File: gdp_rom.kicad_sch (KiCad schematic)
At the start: 19 parts, among them J10 Conn_01x02_Male, J3 Conn_02x25_Counter_Clockwise, J4 Conn_02x25_Counter_Clockwise, U14 74LS05, U18 74LS374, U29 2332A, U39 74LS138, U40 74LS20, U5 74LS08, U6 74LS32, U9 EF936x

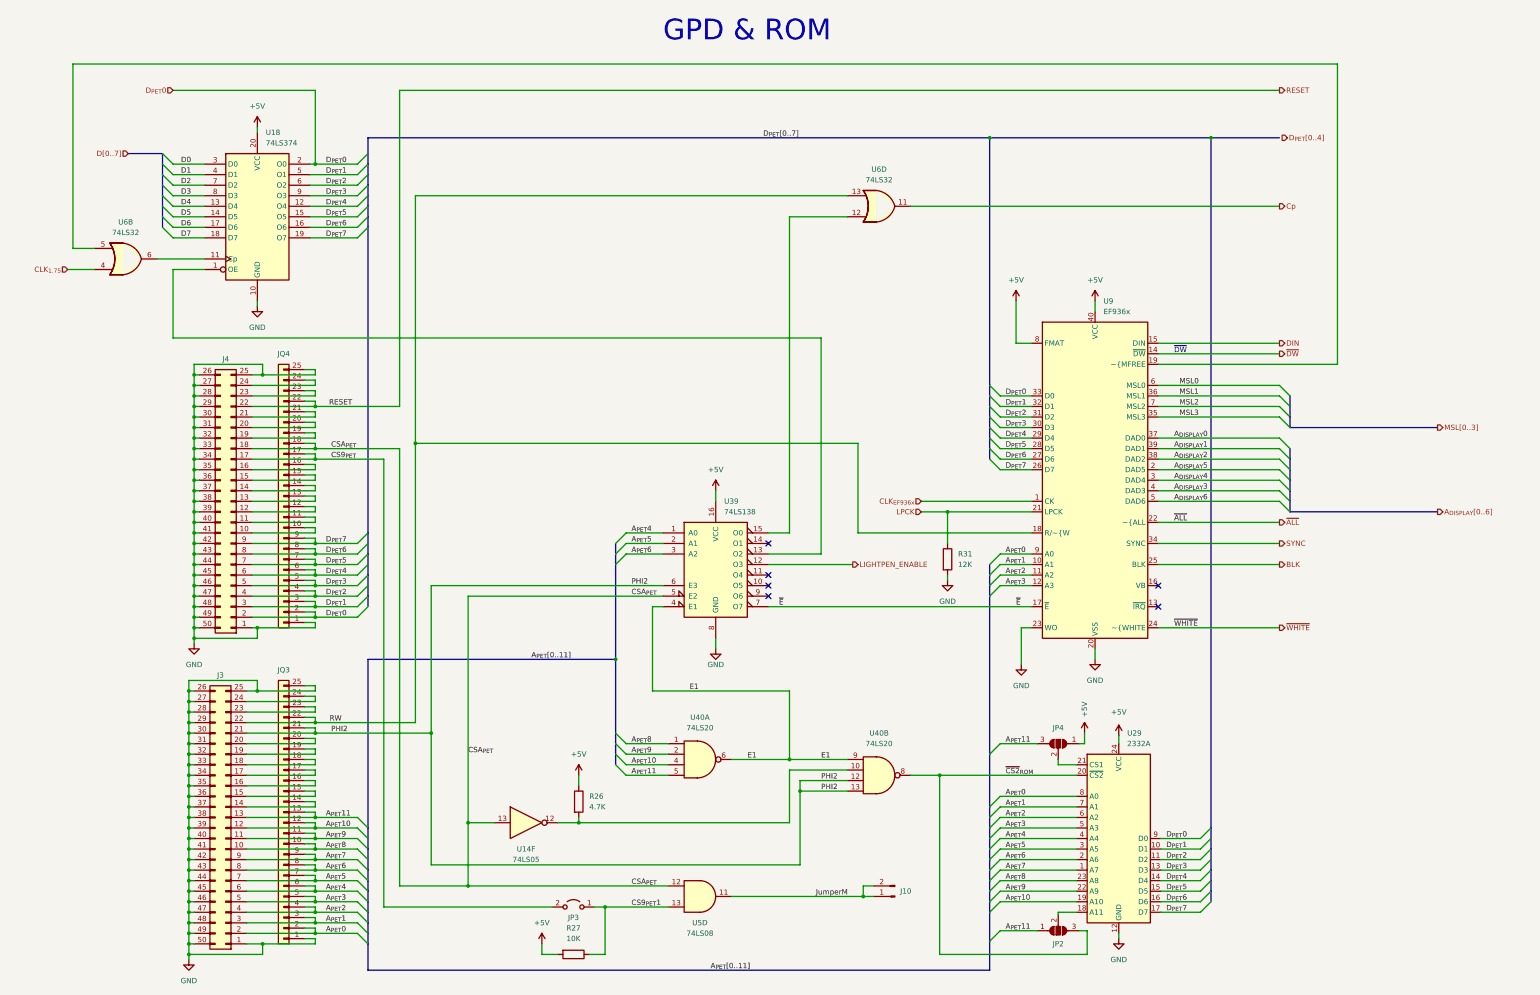
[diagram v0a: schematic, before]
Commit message: Improved signal naming
clearer naming of some signals for better readability
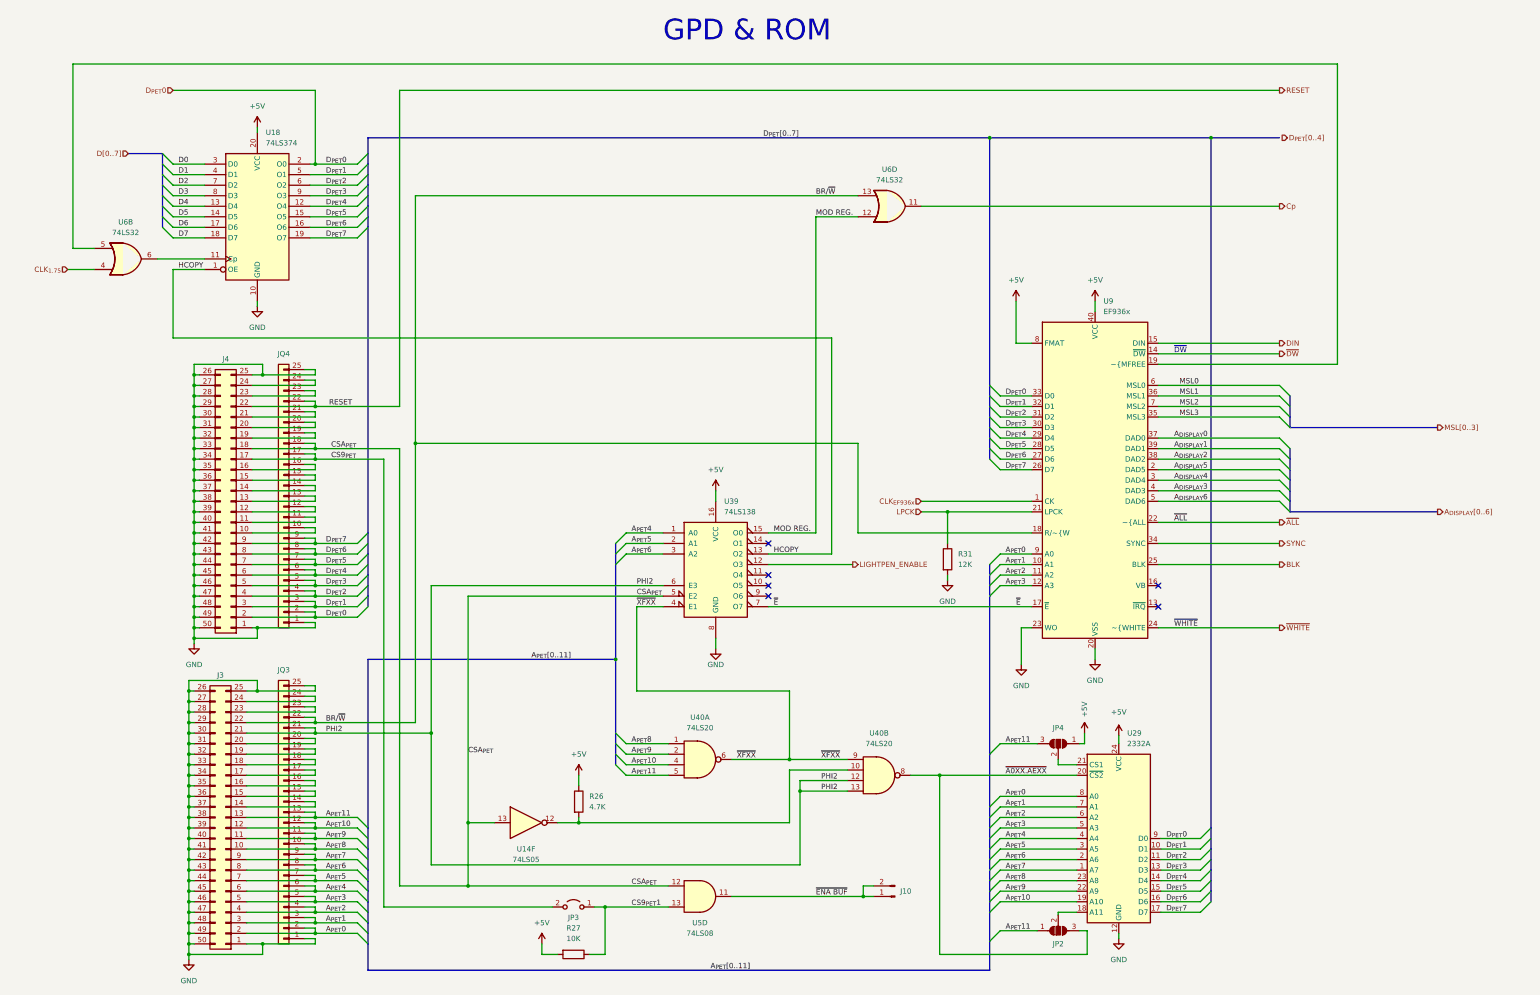
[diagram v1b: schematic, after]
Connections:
- net HCOPY: now reaches U18.1 (OE), U39.13 (O2)
- net MOD REG.: now reaches U39.15 (O0), U6.12
- net E1 renamed ~{XFXX}
- net JumperM renamed ~{ENA BUF}
- net RW renamed BR/~{W}
- net ~{CS2}_{ROM} renamed ~{A0XX.AEXX}
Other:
- moved on the sheet: U6D

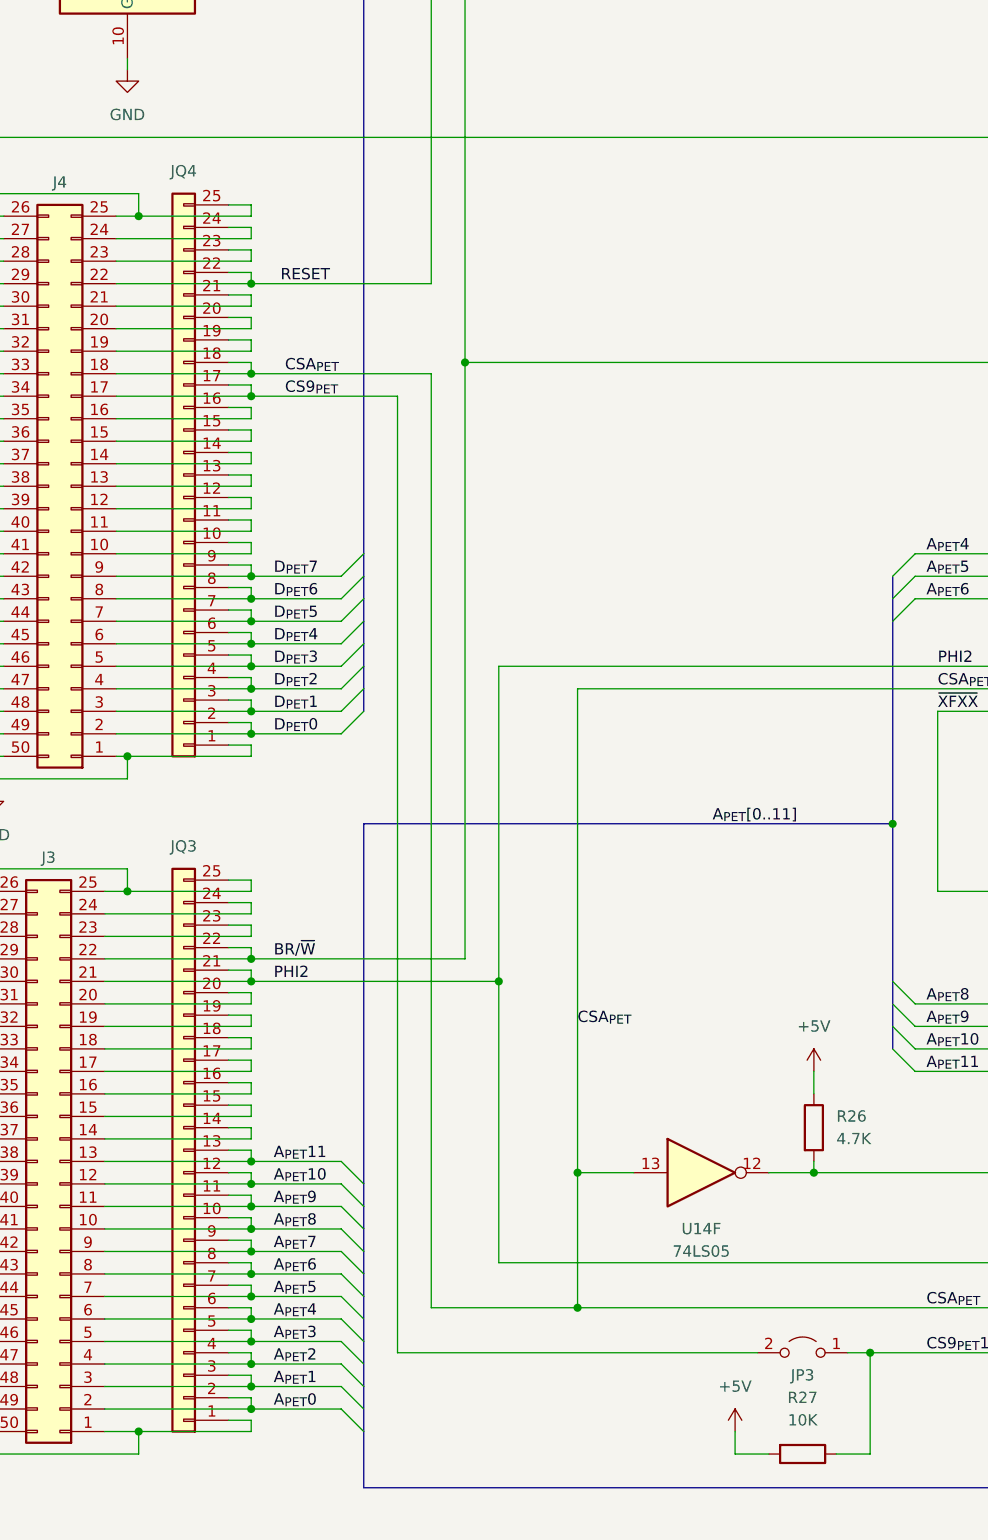
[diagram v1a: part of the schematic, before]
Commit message: kicad drawing sheet fixes
fixed license links in drawing sheets to match board prints, readme and project
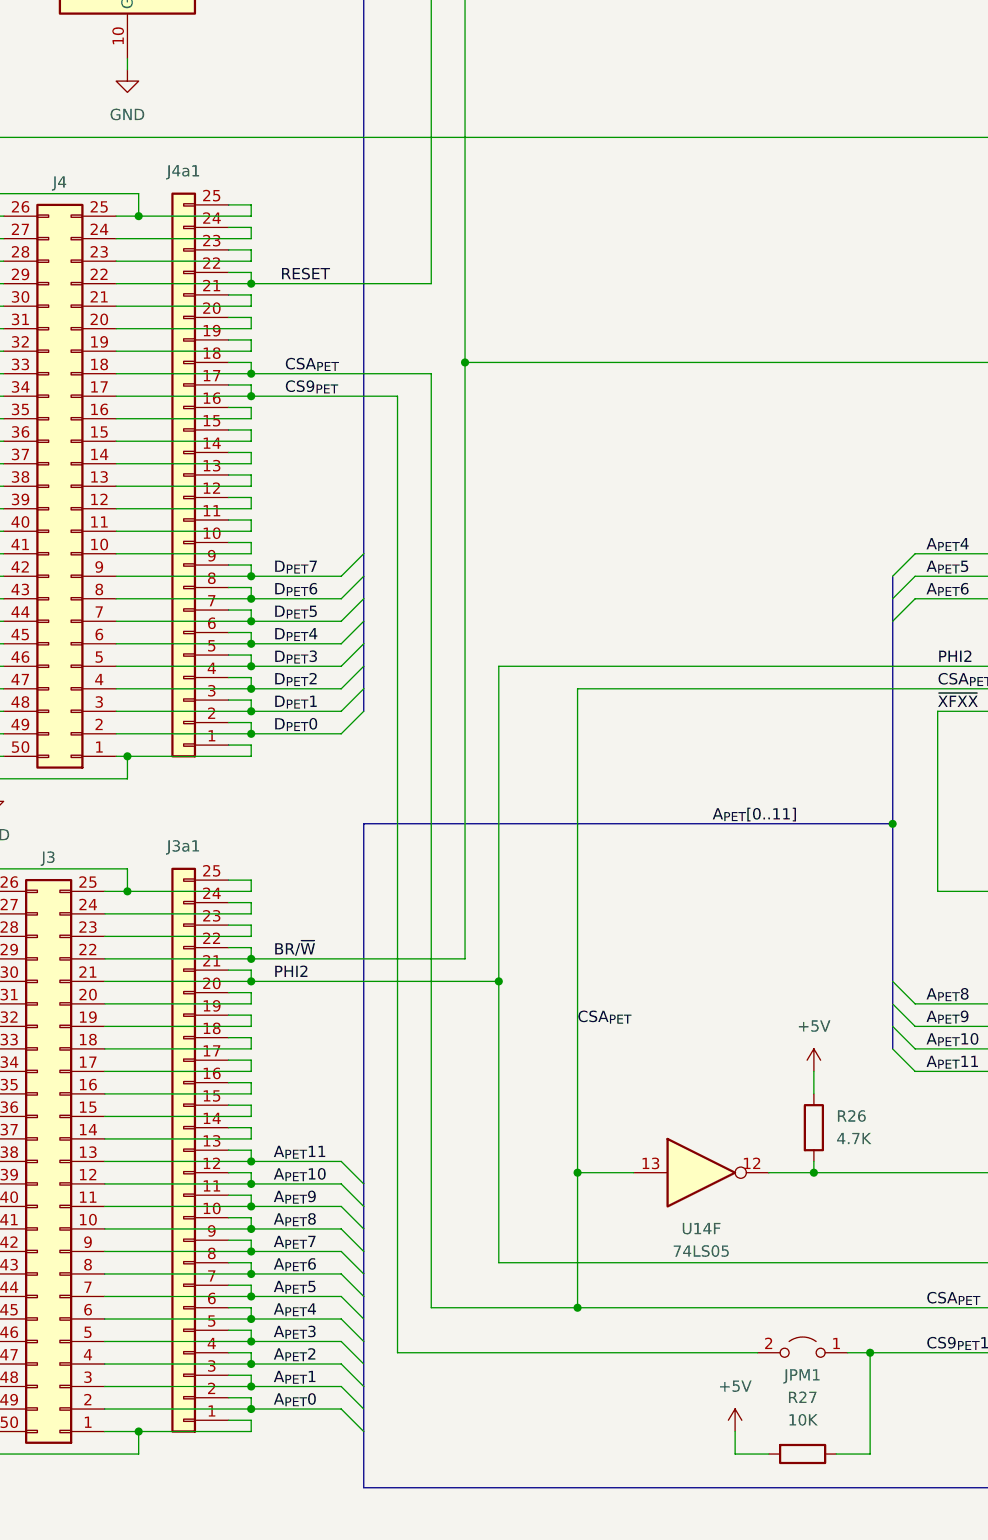
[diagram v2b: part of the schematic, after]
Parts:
- renumbered JQ3 to J3a1, JQ4 to J4a1, JP3 to JPM1
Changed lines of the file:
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@@
     (rev "V001")
     (comment 1 "reverse-engineered in 2022")
-    (comment 2 "creativecommons.org/licenses/by/4.0/")
-    (comment 3 "License: CC BY 4.0")
+    (comment 2 "creativecommons.org/licenses/by-sa/4.0/")
+    (comment 3 "License: CC BY-SA 4.0")
     (comment 4 "Author: InsaneDruid")
   )
@@
   (symbol (lib_id "Jumper:Jumper_2_Open") (at 167.64 237.49 0) (mirror y) (unit 1)
     (in_bom no) (on_board yes) (dnp no)
-    (property "Reference" "JP3" (at 167.64 240.03 0)
+    (property "Reference" "JPM1" (at 167.64 240.03 0)
       (effects (font (size 1.27 1.27)))
     )
@@
       (project "lsg"
         (path "/e63e39d7-6ac0-4ffd-8aa3-1841a4541b55/25c73cf5-2daa-4b48-a85c-af0d7b46ac70"
-          (reference "JP3") (unit 1)
+          (reference "JPM1") (unit 1)
         )
       )
@@
   (symbol (lib_id "Connector_Generic:Conn_01x25") (at 97.79 214.63 180) (unit 1)
     (in_bom yes) (on_board yes) (dnp no) (fields_autoplaced)
-    (property "Reference" "JQ3" (at 97.79 180.34 0)
+    (property "Reference" "J3a1" (at 97.79 180.34 0)
       (effects (font (size 1.27 1.27)))
     )
@@
       (project "lsg"
         (path "/e63e39d7-6ac0-4ffd-8aa3-1841a4541b55/25c73cf5-2daa-4b48-a85c-af0d7b46ac70"
-          (reference "JQ3") (unit 1)
+          (reference "J3a1") (unit 1)
         )
       )
@@
   (symbol (lib_id "Connector_Generic:Conn_01x25") (at 97.79 138.43 180) (unit 1)
     (in_bom yes) (on_board yes) (dnp no) (fields_autoplaced)
-    (property "Reference" "JQ4" (at 97.79 104.14 0)
+    (property "Reference" "J4a1" (at 97.79 104.14 0)
       (effects (font (size 1.27 1.27)))
     )
@@
       (project "lsg"
         (path "/e63e39d7-6ac0-4ffd-8aa3-1841a4541b55/25c73cf5-2daa-4b48-a85c-af0d7b46ac70"
-          (reference "JQ4") (unit 1)
+          (reference "J4a1") (unit 1)
         )
       )
